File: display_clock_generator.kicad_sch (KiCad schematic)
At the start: 12 parts, among them IC14 MC74F241N, IC22 SN74S74N, IC23 HD74S00P

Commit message: pcb: add IC22, IC23, OSC3, OSC4
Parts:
- IC22: footprint (none) -> Package_DIP:DIP-14_W7.62mm
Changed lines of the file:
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@@
       (effects (font (size 1.27 1.27)) (justify left))
     )
-    (property "Footprint" "" (at 95.25 64.77 0)
+    (property "Footprint" "Package_DIP:DIP-14_W7.62mm" (at 95.25 64.77 0)
       (effects (font (size 1.27 1.27)) hide)
     )
@@
       (effects (font (size 1.27 1.27)) (justify left))
     )
-    (property "Footprint" "" (at 49.53 172.72 0)
+    (property "Footprint" "Package_DIP:DIP-14_W7.62mm" (at 49.53 172.72 0)
       (effects (font (size 1.27 1.27)) hide)
     )
@@
       (effects (font (size 1.27 1.27)) (justify left))
     )
-    (property "Footprint" "" (at 95.25 95.25 0)
-      (effects (font (size 1.27 1.27)) hide)
-    )
+    (property "Footprint" "Package_DIP:DIP-14_W7.62mm" (at 95.25 95.25 0)
+      (effects (font (size 1.27 1.27)) hide)
+    )

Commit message: pcb: fix some DRC check errors
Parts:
- R73: footprint (none) -> Resistor_SMD:R_1206_3216Metric
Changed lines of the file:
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@@
       (effects (font (size 1.27 1.27)) (justify left) hide)
     )
-    (property "Footprint" "" (at 215.9 129.54 0)
+    (property "Footprint" "Resistor_SMD:R_1206_3216Metric" (at 215.9 129.54 0)
       (effects (font (size 1.27 1.27)) hide)
     )

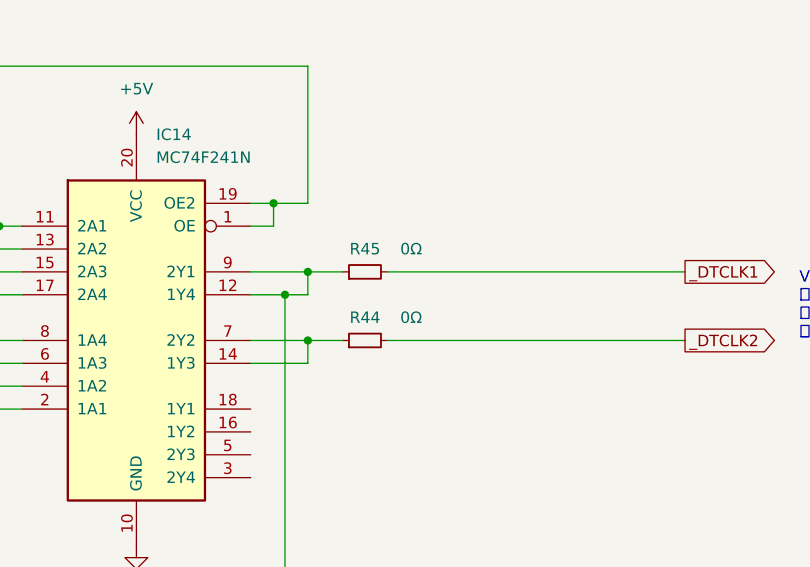
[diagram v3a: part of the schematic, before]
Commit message: pcb: add IC14
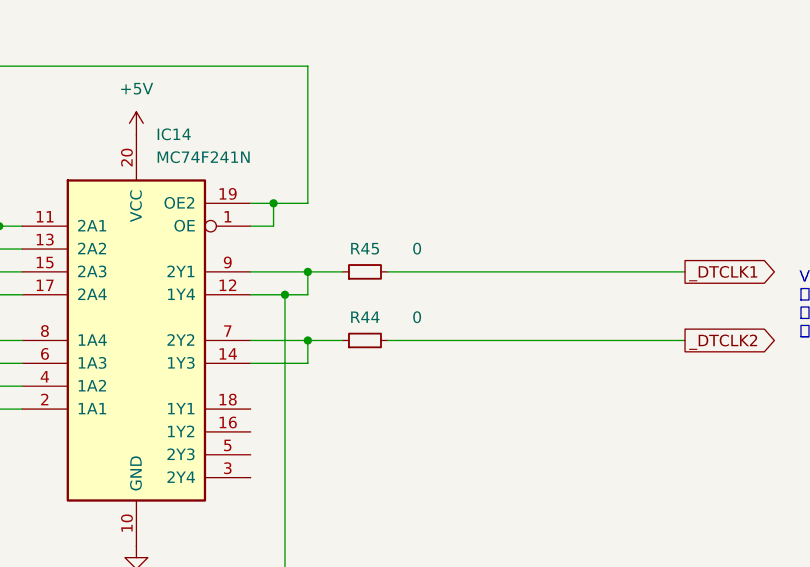
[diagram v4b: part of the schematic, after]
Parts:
- IC14: footprint (none) -> Package_DIP:DIP-20_W7.62mm
- R44, R45: value 0Ω -> 0; footprint (none) -> Resistor_SMD:R_1206_3216Metric
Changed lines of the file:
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@@
       (effects (font (size 1.27 1.27)) (justify left))
     )
-    (property "Footprint" "" (at 182.88 72.39 0)
+    (property "Footprint" "Package_DIP:DIP-20_W7.62mm" (at 182.88 72.39 0)
       (effects (font (size 1.27 1.27)) hide)
     )
@@
       (effects (font (size 1.27 1.27)))
     )
-    (property "Value" "0Ω" (at 214.63 64.77 90)
-      (effects (font (size 1.27 1.27)) (justify left))
-    )
-    (property "Footprint" "" (at 208.28 67.31 0)
+    (property "Value" "0" (at 214.63 64.77 90)
+      (effects (font (size 1.27 1.27)) (justify left))
+    )
+    (property "Footprint" "Resistor_SMD:R_1206_3216Metric" (at 208.28 67.31 0)
       (effects (font (size 1.27 1.27)) hide)
     )
@@
       (effects (font (size 1.27 1.27)))
     )
-    (property "Value" "0Ω" (at 214.63 72.39 90)
-      (effects (font (size 1.27 1.27)) (justify left))
-    )
-    (property "Footprint" "" (at 208.28 74.93 0)
-      (effects (font (size 1.27 1.27)) hide)
-    )
+    (property "Value" "0" (at 214.63 72.39 90)
+      (effects (font (size 1.27 1.27)) (justify left))
+    )
+    (property "Footprint" "Resistor_SMD:R_1206_3216Metric" (at 208.28 74.93 0)
+      (effects (font (size 1.27 1.27)) hide)
+    )

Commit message: pcb: wiring IC1 to TEXT BUS
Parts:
- R69, R70: footprint (none) -> Resistor_SMD:R_1206_3216Metric
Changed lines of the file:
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@@
       (effects (font (size 1.27 1.27)) (justify left) hide)
     )
-    (property "Footprint" "" (at 80.01 41.91 0)
+    (property "Footprint" "Resistor_SMD:R_1206_3216Metric" (at 80.01 41.91 0)
       (effects (font (size 1.27 1.27)) hide)
     )
@@
       (effects (font (size 1.27 1.27)) (justify left) hide)
     )
-    (property "Footprint" "" (at 158.75 29.21 0)
-      (effects (font (size 1.27 1.27)) hide)
-    )
+    (property "Footprint" "Resistor_SMD:R_1206_3216Metric" (at 158.75 29.21 0)
+      (effects (font (size 1.27 1.27)) hide)
+    )

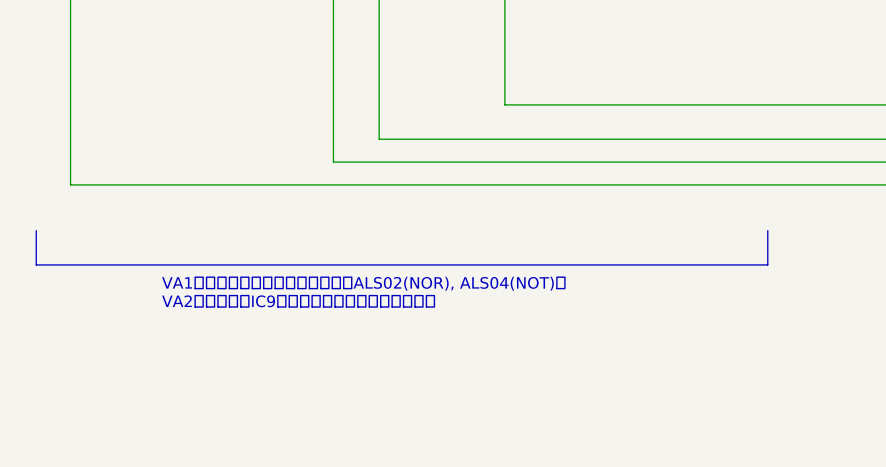
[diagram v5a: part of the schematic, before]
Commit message: schematic: tidy hierarchical sheets
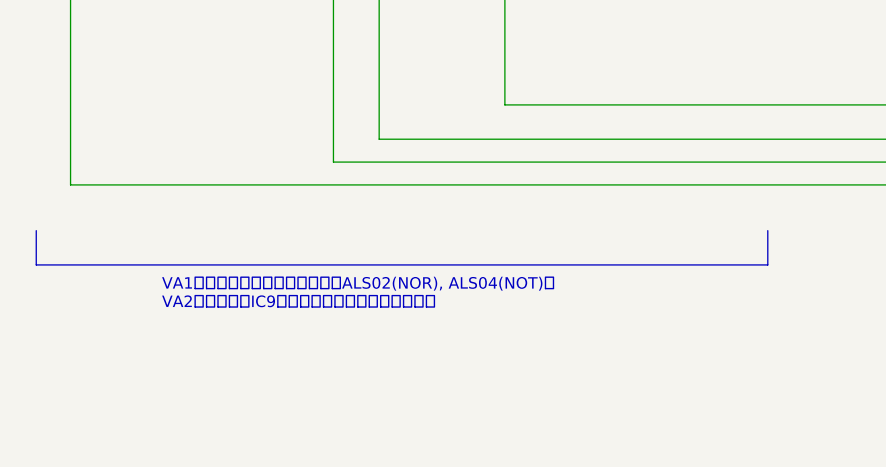
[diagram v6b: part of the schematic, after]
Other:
- note added: "VA1回路図でこの辺りに存在するALS02(NOR), ALS04(NOT)は VA2には無く、IC9からの信号が直結されている。"
- note removed: "VA1回路図ではこの辺りに存在するALS02(NOR), ALS04(NOT)は VA2には無く、IC9からの信号が直結されている。"
- title: ディスプレイ・クロック・ジェネレータ -> ディスプレイクロック ジェネレータ
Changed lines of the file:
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@@
   (paper "A4")
   (title_block
-    (title "ディスプレイ・クロック・ジェネレータ")
-    (comment 1 "VA1回路図 P.262")
+    (title "ディスプレイクロック ジェネレータ")
+    (comment 1 "VA1回路図 P.263")
   )
   (junction (at 201.93 74.93) (diameter 0) (color 0 0 0 0)
@@
     (effects (font (size 1.27 1.27)) (justify left bottom))
   )
-  (text "VA1回路図ではこの辺りに存在するALS02(NOR), ALS04(NOT)は\nVA2には無く、IC9からの信号が直結されている。"
+  (text "VA1回路図でこの辺りに存在するALS02(NOR), ALS04(NOT)は\nVA2には無く、IC9からの信号が直結されている。"
     (at 105.41 176.53 0)
     (effects (font (size 1.27 1.27)) (justify left bottom))
